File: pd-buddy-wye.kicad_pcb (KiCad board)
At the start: 2 copper layers, 16.9 x 25 mm, 7 parts, among them J1 Power, J2 UFP, P1 DFP+Power

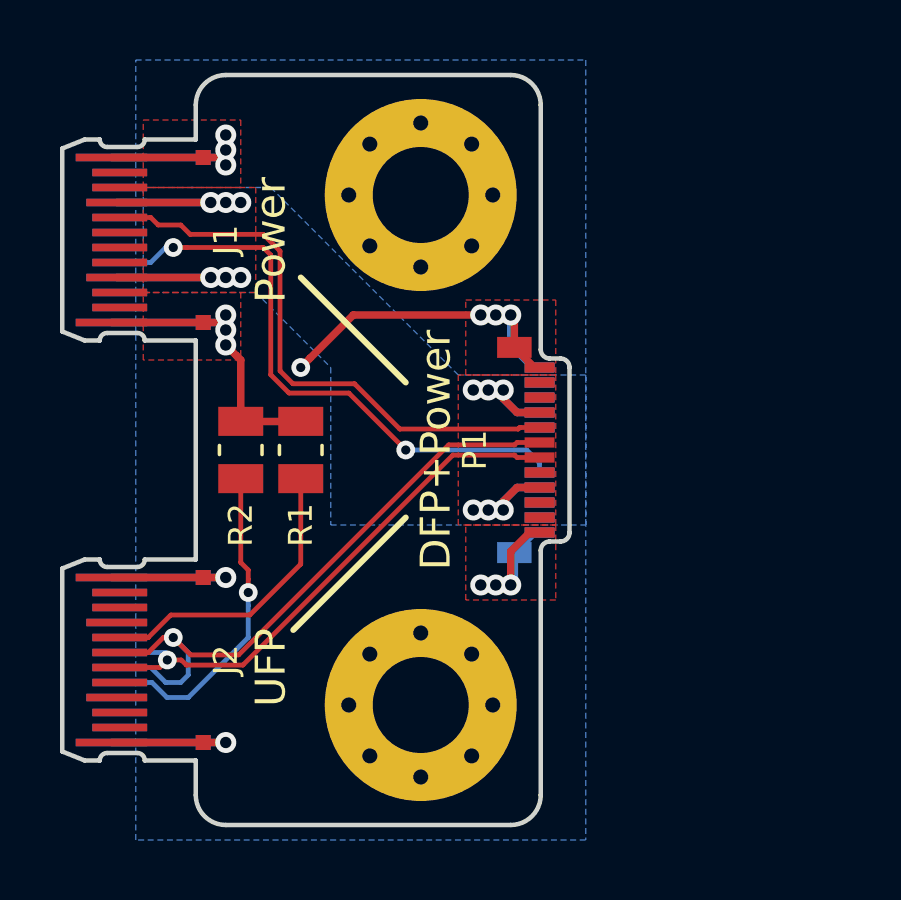
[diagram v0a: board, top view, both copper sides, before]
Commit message: Update to KiCad 8 and add PDF
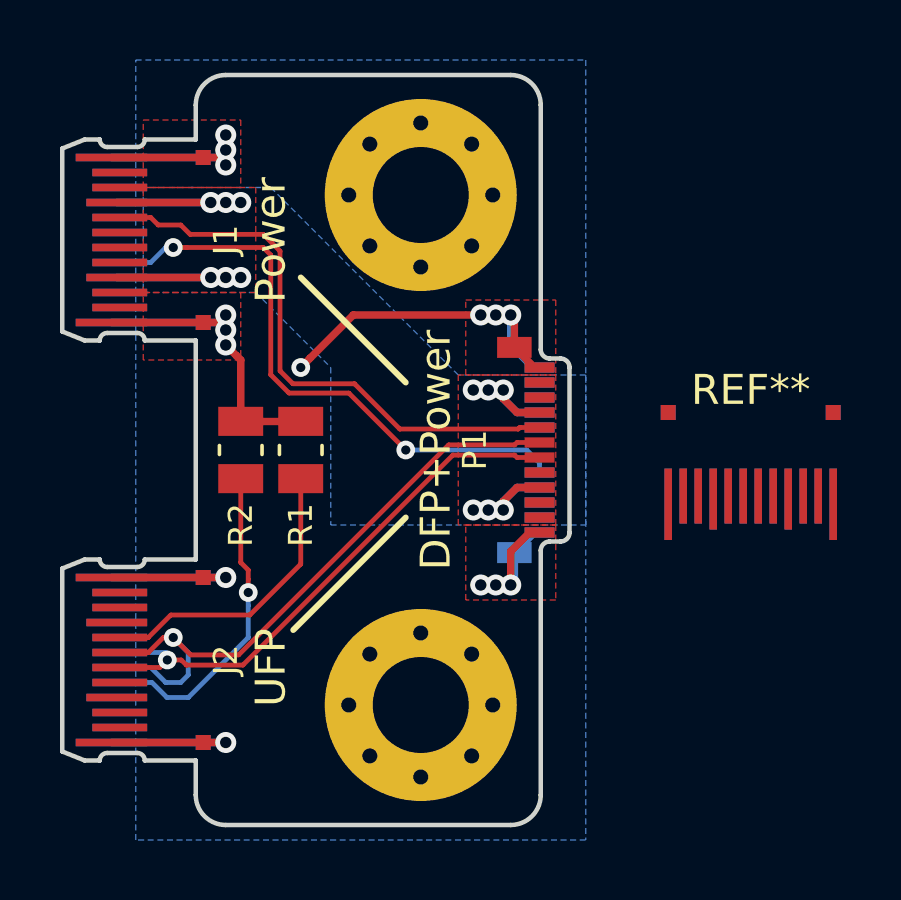
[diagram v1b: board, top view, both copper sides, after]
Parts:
- added REF**: USB_C_Receptacle_PCBEdge_Alt, Connector_USB_C_PCBEdge:USB_C_Receptacle_PCBEdge_Alt_ShieldPads, F.Cu at (126.0, 111.5)
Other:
- net class Default removed
- net class Power removed
- net class Power_Small removed
